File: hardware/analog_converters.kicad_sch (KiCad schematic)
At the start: 16 parts, among them U3 INA229, U4 INA281A5

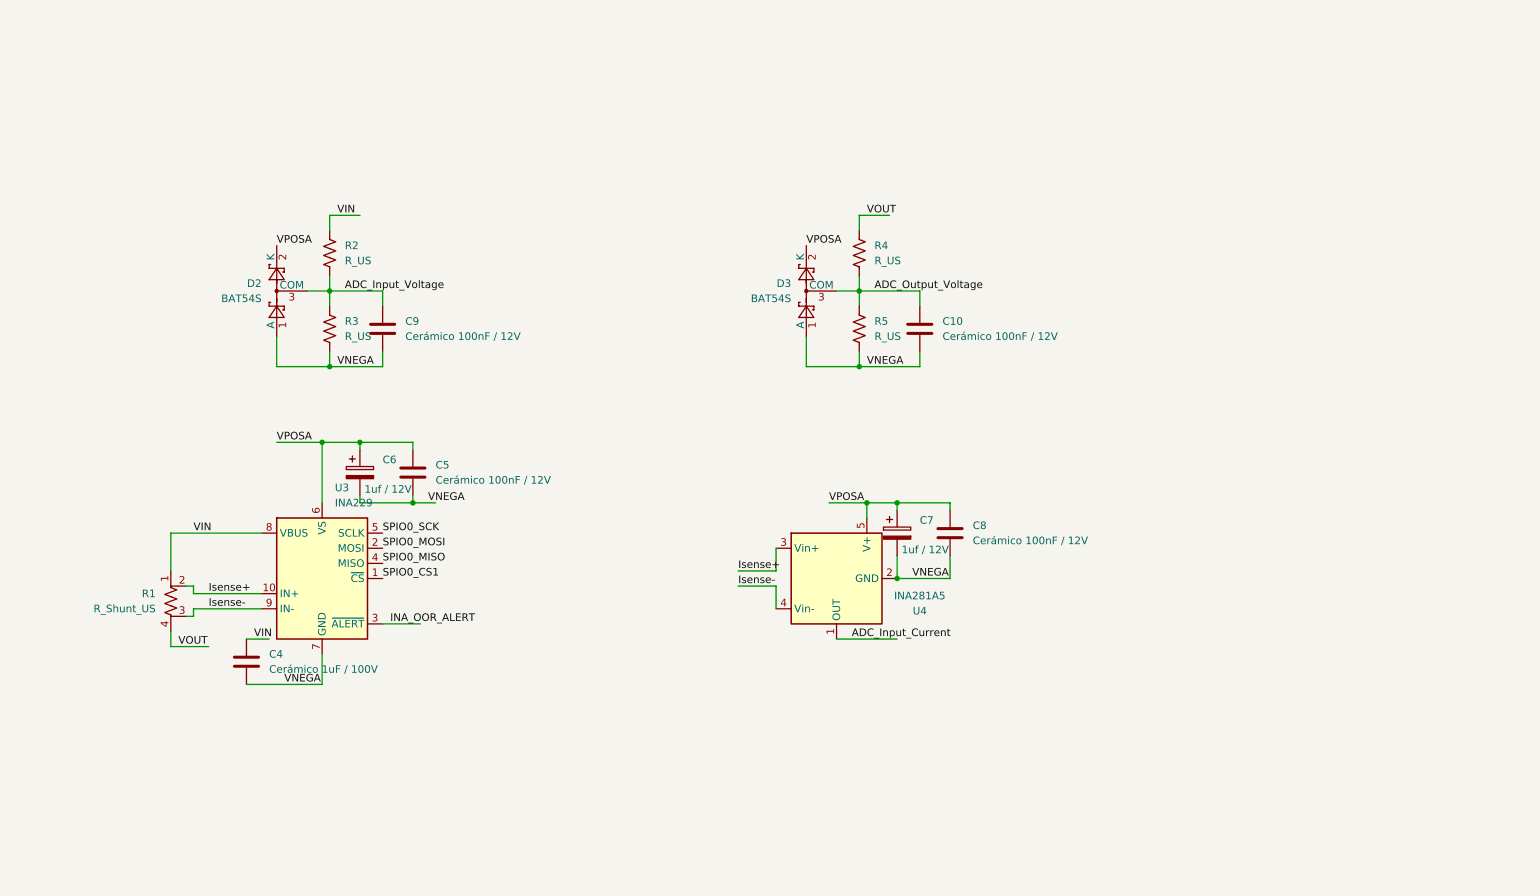
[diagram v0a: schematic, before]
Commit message: HW: Footprints, Descriptions and LCSC part number added to sch
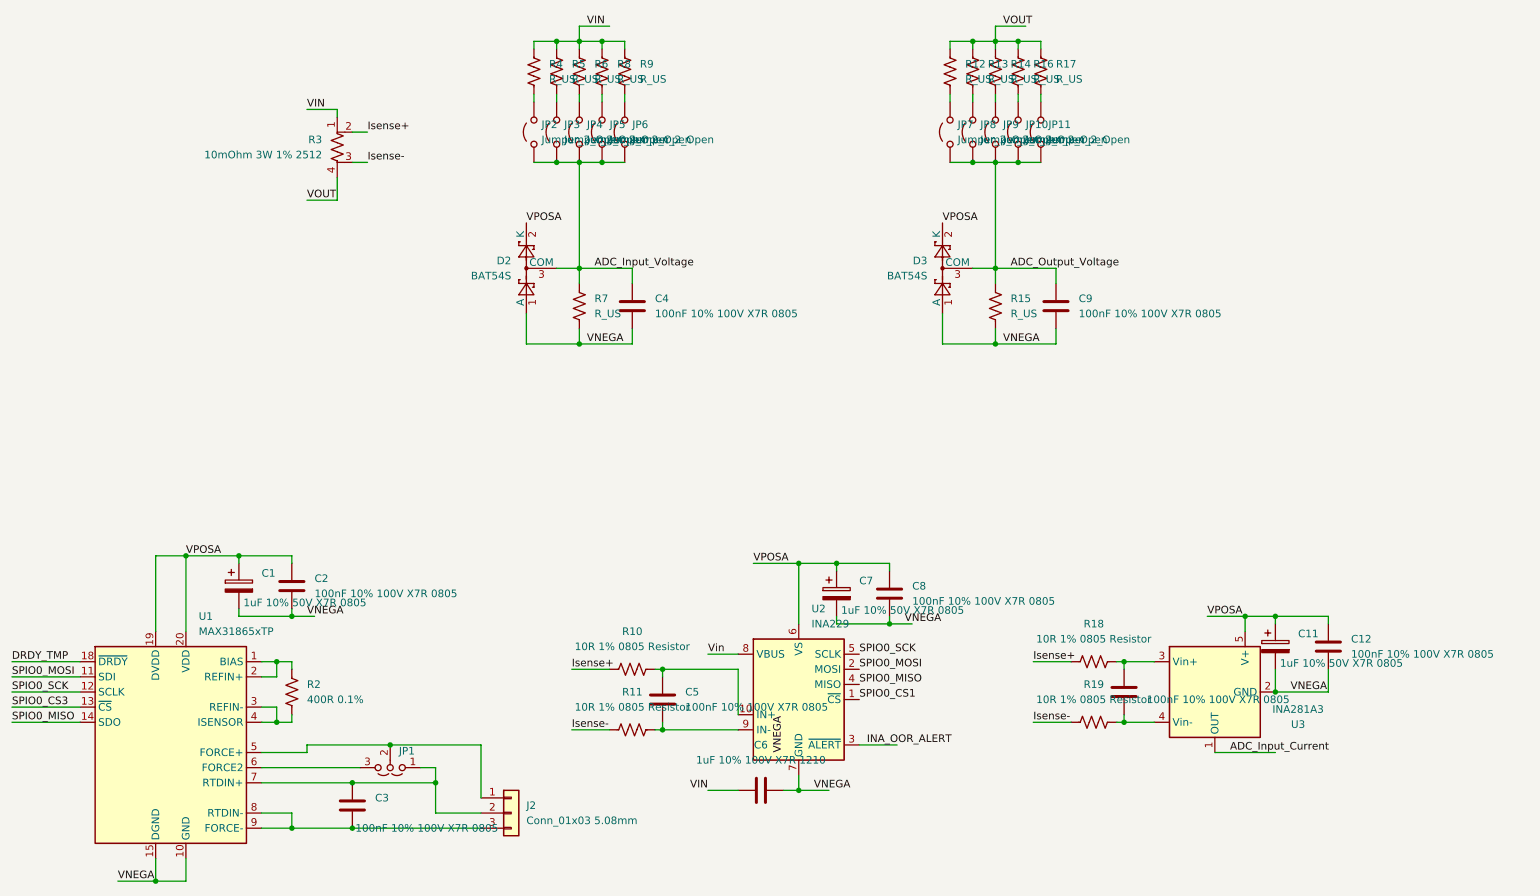
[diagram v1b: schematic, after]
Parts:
- added C1: 1uF 10% 50V X7R 0805, Capacitor_SMD:C_0805_2012Metric_Pad1.18x1.45mm_HandSolder, symbol Device:C_Polarized
- added C10, C2, C3, C5: 100nF 10% 100V X7R 0805, Capacitor_SMD:C_0805_2012Metric_Pad1.18x1.45mm_HandSolder, symbol Device:C
- added J2: Conn_01x03 5.08mm, TerminalBlock_Phoenix:TerminalBlock_Phoenix_MKDS-1,5-3-5.08_1x03_P5.08mm_Horizontal, symbol Connector_Generic:Conn_01x03
- added JP1: 2/3 Wire Selector, Connector_PinHeader_2.54mm:PinHeader_1x03_P2.54mm_Vertical, symbol Jumper:Jumper_3_Open
- added JP10, JP11, JP2, JP3, JP4, JP5, JP6, JP7, JP8, JP9: Jumper_2_Open, Connector_PinHeader_2.54mm:PinHeader_1x02_P2.54mm_Vertical, symbol Jumper:Jumper_2_Open
- added R10, R11, R18, R19: 10R 1% 0805 Resistor, Resistor_SMD:R_0805_2012Metric_Pad1.20x1.40mm_HandSolder, symbol Device:R_US
- added R12, R13, R14, R16, R17, R5, R6, R8, R9: R_US, Resistor_SMD:R_0805_2012Metric_Pad1.20x1.40mm_HandSolder, symbol Device:R_US
- added U1: MAX31865xTP, Package_DFN_QFN:TQFN-20-1EP_5x5mm_P0.65mm_EP3.25x3.25mm, symbol Sensor_Temperature:MAX31865xTP
- C11: renamed from C7; value 1uf / 12V -> 1uF 10% 50V X7R 0805; footprint (none) -> Capacitor_SMD:C_0805_2012Metric_Pad1.18x1.45mm_HandSolder; LCSC Part (none) -> C77083
- C12: renamed from C8; value Cerámico 100nF / 12V -> 100nF 10% 100V X7R 0805; footprint (none) -> Capacitor_SMD:C_0805_2012Metric_Pad1.18x1.45mm_HandSolder; LCSC Part (none) -> C28233
- C4: renamed from C9; value Cerámico 100nF / 12V -> 100nF 10% 100V X7R 0805; footprint (none) -> Capacitor_SMD:C_0805_2012Metric_Pad1.18x1.45mm_HandSolder; LCSC Part (none) -> C28233
- C6: renamed from C4; value Cerámico 1uF / 100V -> 1uF 10% 100V X7R 1210; footprint (none) -> Capacitor_SMD:C_1210_3225Metric_Pad1.33x2.70mm_HandSolder; LCSC Part (none) -> C382212
- C7: renamed from C6; value 1uf / 12V -> 1uF 10% 50V X7R 0805; footprint (none) -> Capacitor_SMD:C_0805_2012Metric_Pad1.18x1.45mm_HandSolder; LCSC Part (none) -> C77083
- C8: renamed from C5; value Cerámico 100nF / 12V -> 100nF 10% 100V X7R 0805; footprint (none) -> Capacitor_SMD:C_0805_2012Metric_Pad1.18x1.45mm_HandSolder; LCSC Part (none) -> C28233
- C9: renamed from C10; value Cerámico 100nF / 12V -> 100nF 10% 100V X7R 0805; footprint (none) -> Capacitor_SMD:C_0805_2012Metric_Pad1.18x1.45mm_HandSolder; LCSC Part (none) -> C28233
- D2, D3: LCSC Part (none) -> C19726
- R15: renamed from R5; footprint (none) -> Resistor_SMD:R_0805_2012Metric_Pad1.20x1.40mm_HandSolder
- R2: value R_US -> 400R 0.1%; footprint (none) -> Resistor_SMD:R_0805_2012Metric_Pad1.20x1.40mm_HandSolder; LCSC Part (none) -> C153298
- R3: renamed from R1; value R_Shunt_US -> 10mOhm 3W 1% 2512; footprint (none) -> Resistor_SMD:R_Shunt_Vishay_WSK2512_6332Metric_T1.19mm; LCSC Part (none) -> C840621
- R4: footprint (none) -> Resistor_SMD:R_0805_2012Metric_Pad1.20x1.40mm_HandSolder
- R7: renamed from R3; footprint (none) -> Resistor_SMD:R_0805_2012Metric_Pad1.20x1.40mm_HandSolder
- U2: renamed from U3; LCSC Part (none) -> C2846803
- U3: renamed from U4; value INA281A5 -> INA281A3; LCSC Part (none) -> C1517407
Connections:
- net ADC_Input_Voltage: now also JP2.1 (A), JP3.1 (A), JP4.1 (A), JP5.1 (A), JP6.1 (A); no longer R2.2
- net ADC_Output_Voltage: now also JP10.1 (A), JP11.1 (A), JP7.1 (A), JP8.1 (A), JP9.1 (A); no longer R4.2
- net Isense+: now also R10.1, R18.1; no longer U2.10 (IN+), U3.3 (Vin+)
- net Isense-: now also R11.1, R19.1; no longer U2.9 (IN-), U3.4 (Vin-)
- net SPIO0_MISO: now also U1.14 (SDO)
- net SPIO0_MOSI: now also U1.11 (SDI)
- net SPIO0_SCK: now also U1.12 (SCLK)
- net VIN: now also R4.1, R5.1, R6.1, R8.1, R9.1; no longer R2.1, U2.8 (VBUS)
- net VNEGA: now also C1.2, C2.2, U1.10 (GND), U1.15 (DGND), U1.16 (GND), U1.21 (GND)
- net VOUT: now also R12.1, R13.1, R14.1, R16.1, R17.1; no longer R4.1
- net VPOSA: now also C1.1, C2.1, U1.19 (DVDD), U1.20 (VDD)
- new net: JP5.2 (B), R8.2
- new net: R2.2, U1.1 (BIAS), U1.2 (REFIN+)
- new net: R2.1, U1.3 (REFIN-), U1.4 (ISENSOR)
- new net: J2.1 (Pin_1), JP1.2 (C), U1.5 (FORCE+)
- new net: JP1.3 (B), U1.6 (FORCE2)
- new net: C3.1, J2.2 (Pin_2), JP1.1 (A), U1.7 (RTDIN+)
- new net: C3.2, J2.3 (Pin_3), U1.8 (RTDIN-), U1.9 (FORCE-)
- new net: C5.1, R10.2, U2.10 (IN+)
- new net: C5.2, R11.2, U2.9 (IN-)
- new net: JP8.2 (B), R13.2
- new net: C10.1, R18.2, U3.3 (Vin+)
- new net: C10.2, R19.2, U3.4 (Vin-)
- new net: JP3.2 (B), R5.2
- new net: JP4.2 (B), R6.2
- new net: JP2.2 (B), R4.2
- new net: JP10.2 (B), R16.2
- new net: JP9.2 (B), R14.2
- new net: JP6.2 (B), R9.2
- new net: JP11.2 (B), R17.2
- new net: JP7.2 (B), R12.2
- new net DRDY_TMP: U1.18 (~{DRDY})
- new net SPIO0_CS3: U1.13 (~{CS})
- new net Vin: U2.8 (VBUS)
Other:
- moved on the sheet: C11, C12, C4, C6, C7, C8, C9, D2, D3, R15, R3, R7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
